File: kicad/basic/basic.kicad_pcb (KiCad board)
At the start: 2 copper layers, 50 x 50 mm, 20 parts, among them P2 CONN_01X15, P3 CONN_01X15, P4 CONN_01X06, P5 CONN_01X01, P6 CONN_01X01, P7 CONN_01X01, P8 CONN_01X01, P9 CONN_01X06, SW1 SW_PUSH, SW2 SW_PUSH

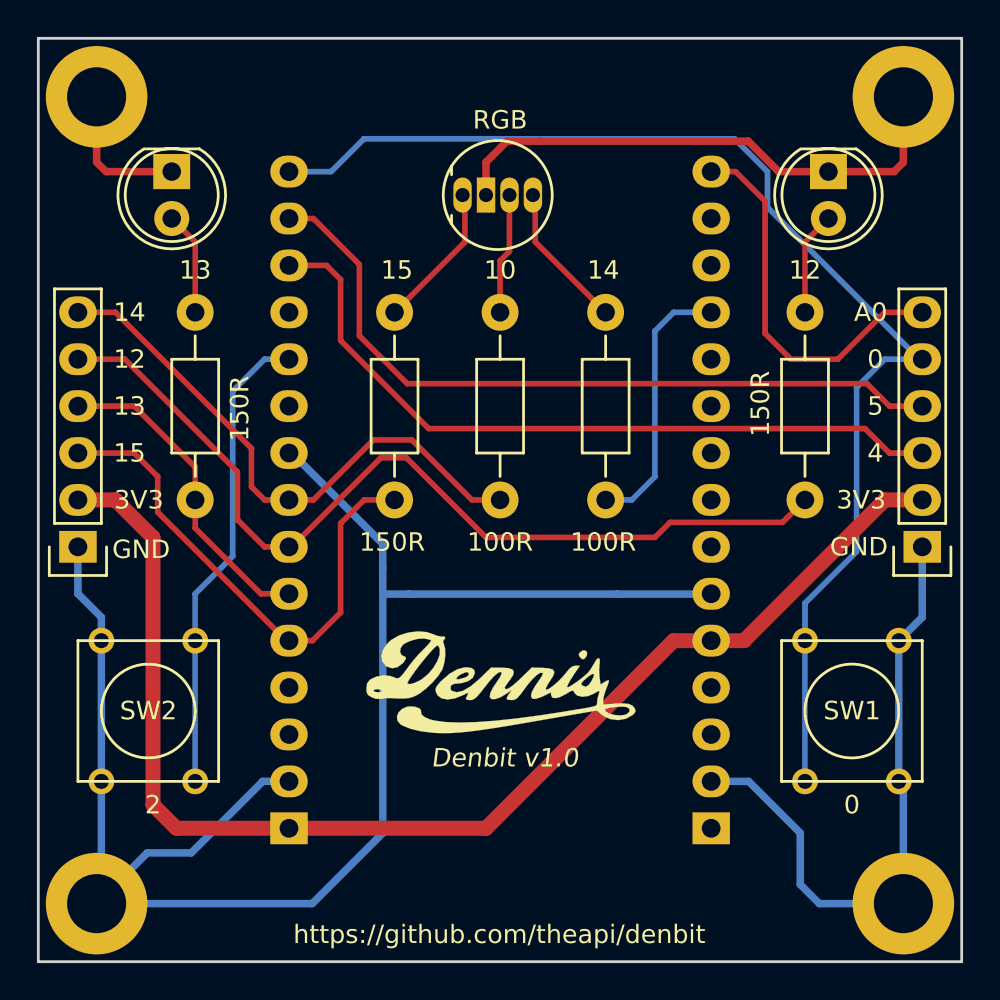
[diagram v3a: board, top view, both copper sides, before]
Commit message: Swap SDA & SCL on the header
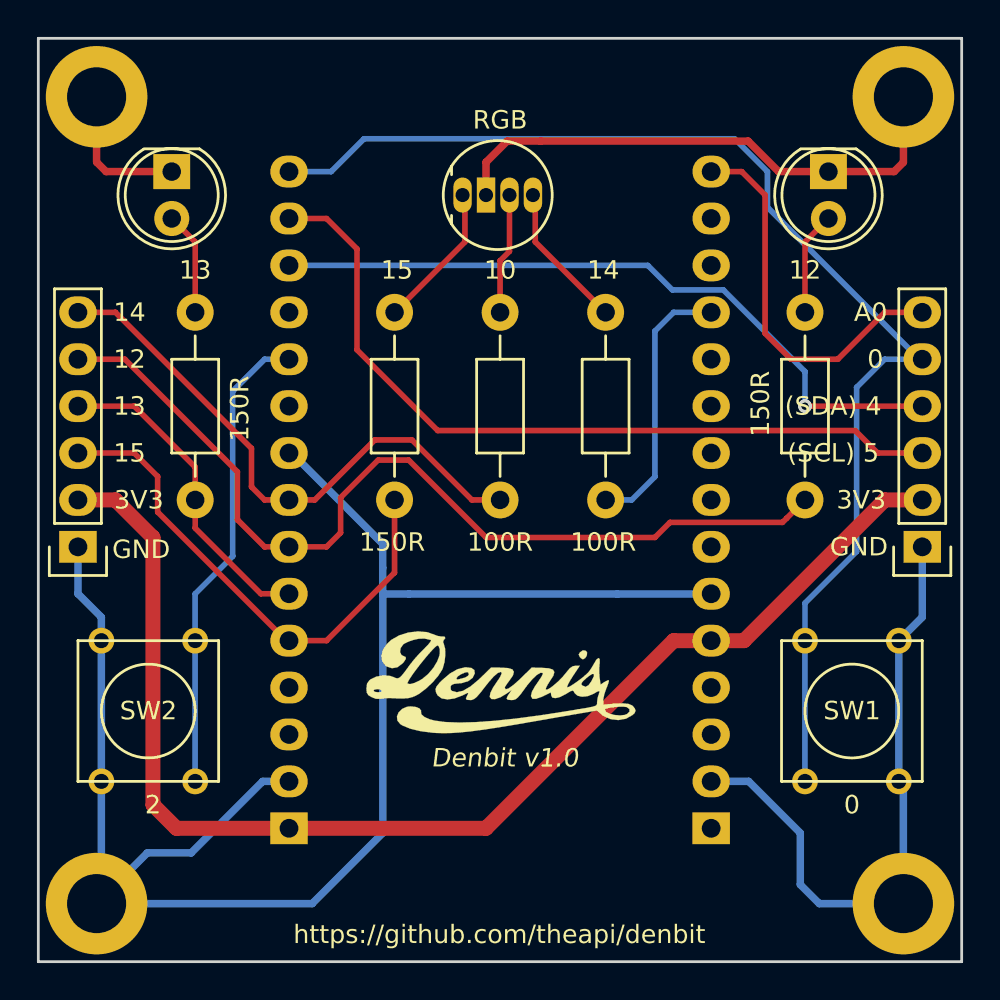
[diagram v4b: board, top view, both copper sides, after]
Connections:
- P4 pad 3: GPIO4 -> GPIO5
- P4 pad 4: GPIO5 -> GPIO4
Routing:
- net GPIO5: track 40.9 -> 42.9 mm
- net GPIO4: track 40.4 -> 38.5 mm, vias 0 -> 1
- net GPIO12: track 49.7 -> 51.1 mm
- net GPIO15: track 29.2 -> 28.1 mm
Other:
- board text added: "(SCL) 5"
- board text added: "(SDA) 4"
- board text removed: "4"
- board text removed: "5"

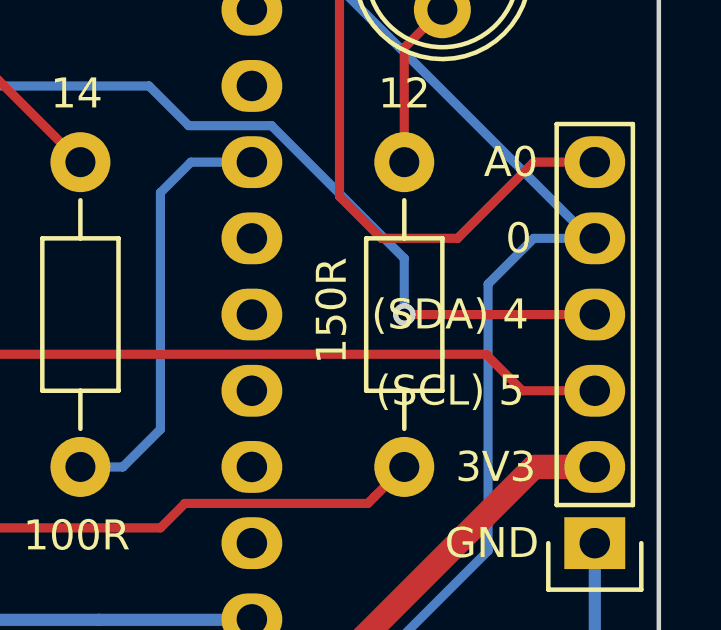
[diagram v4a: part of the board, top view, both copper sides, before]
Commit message: Tweaked labels
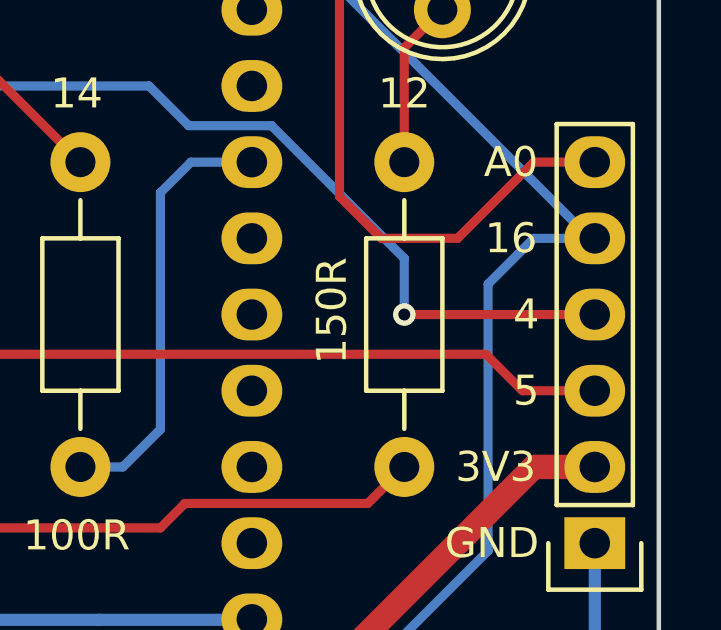
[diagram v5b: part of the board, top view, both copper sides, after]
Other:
- board text added: "16"
- board text added: "4"
- board text added: "5"
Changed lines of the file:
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@@
-(kicad_pcb (version 4) (host pcbnew 4.0.2-4+6225~38~ubuntu14.04.1-stable)
+(kicad_pcb (version 4) (host pcbnew 4.0.1-stable)
   (general
     (links 41)
     (no_connects 0)
-    (area 115.226999 66.712999 175.427001 126.913001)
+    (area 120.251999 71.737999 170.402001 121.888001)
     (thickness 1.6)
     (drawings 73)
@@
       (xy 4.255281 -1.532513) (xy 4.318 -1.651) (xy 4.481568 -1.764619) (xy 4.636344 -1.746168)) (layer F.SilkS) (width 0.01))
   )
-  (gr_text "(SDA) 4" (at 163.366 91.73) (layer F.SilkS)
+  (gr_text 4 (at 165.906 91.73) (layer F.SilkS)
     (effects (font (size 1 1) (thickness 0.15)))
   )
@@
     (effects (font (size 1 1) (thickness 0.15)) (justify mirror))
   )
-  (gr_text 0 (at 165.652 89.19) (layer B.SilkS)
+  (gr_text 16 (at 165.652 89.19) (layer B.SilkS)
     (effects (font (size 1 1) (thickness 0.15)) (justify mirror))
   )
@@
     (effects (font (size 1 1) (thickness 0.15)))
   )
-  (gr_text 0 (at 165.652 89.19) (layer F.SilkS)
+  (gr_text 16 (at 165.398 89.19) (layer F.SilkS)
     (effects (font (size 1 1) (thickness 0.15)))
   )
@@
     (effects (font (size 1 1) (thickness 0.15)) (justify mirror))
   )
-  (gr_text "(SCL) 5" (at 163.366 94.27) (layer F.SilkS)
-    (effects (font (size 1 1) (thickness 0.15)))
-  )
+  (gr_text 5 (at 165.906 94.27) (layer F.SilkS)
+    (effects (font (size 1 1) (thickness 0.15)))
+  )

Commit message: External power
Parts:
- added P1: EXT_PWR, Pin_Headers:Pin_Header_Straight_1x02, F.Cu at (144.1, 117.1)
- moved G*** 3.56 mm to (145.3, 103.2)
- moved G*** 1.02 mm to (145.3, 105.7)
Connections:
- P2 pad 1: Net-(P2-Pad1) -> VIN
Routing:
- net GND: track 164.4 -> 180.7 mm
- net VIN: track 0.00 -> 11.2 mm
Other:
- board text added: "4.5-10V"
- board text added: "ALT_PWR"

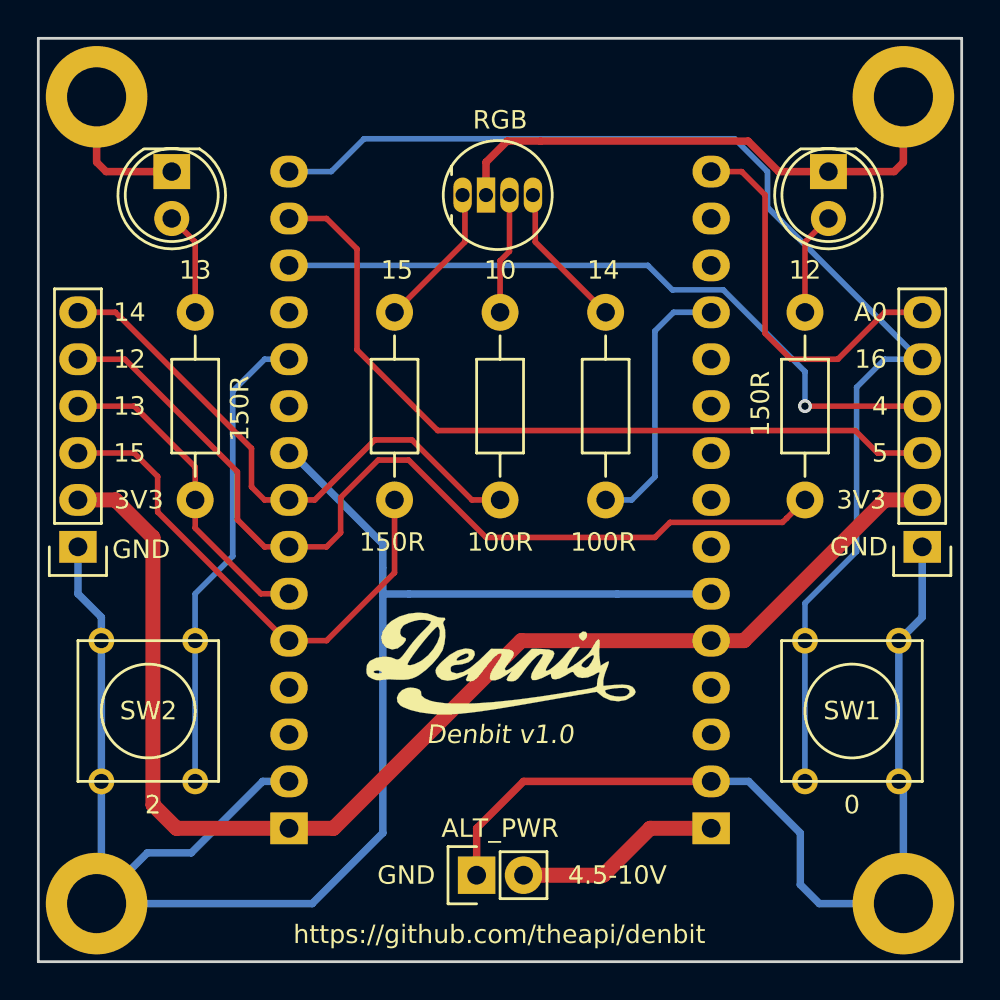
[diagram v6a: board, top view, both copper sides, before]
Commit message: Led position tweak & silkscreen adjustments
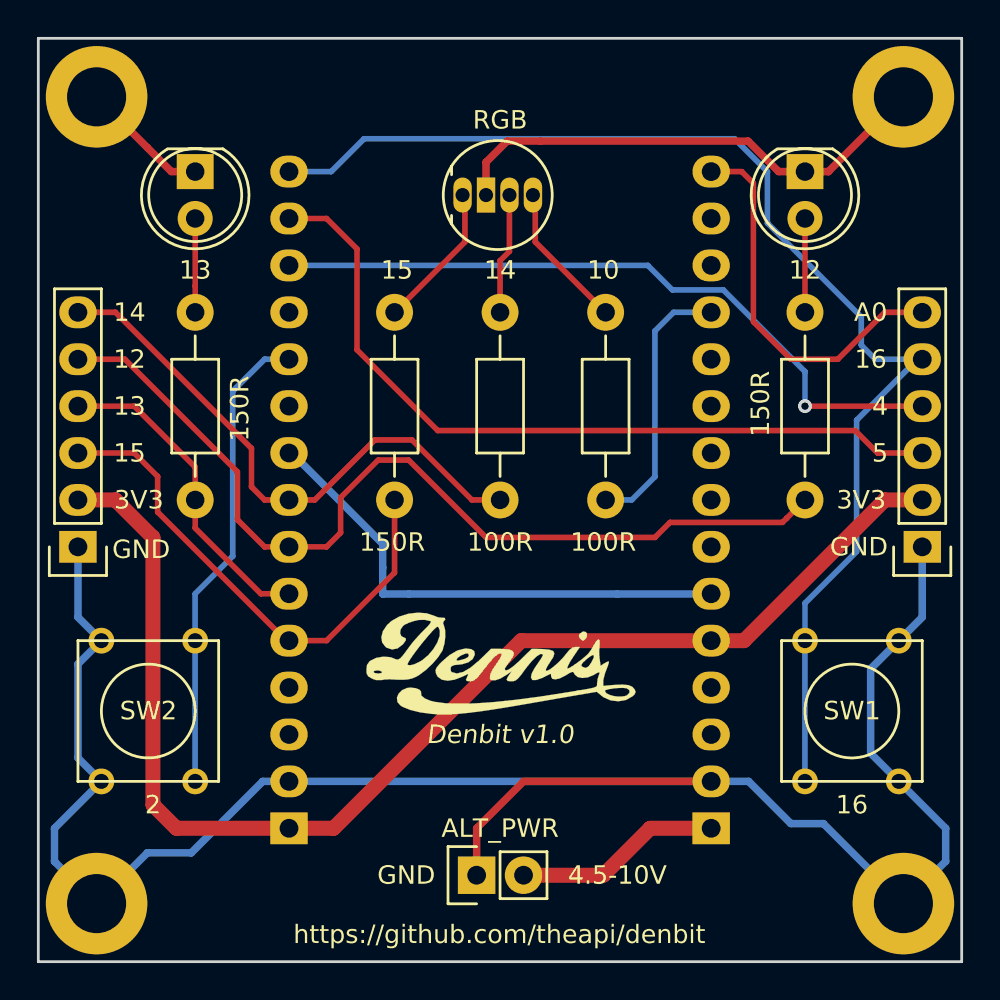
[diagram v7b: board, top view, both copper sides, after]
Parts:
- moved D1 1.27 mm to (128.8, 79.0)
- moved D4 1.27 mm to (161.8, 79.0)
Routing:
- net GND: track 180.7 -> 175.1 mm
- net /S_GREEN: track 5.61 -> 5.08 mm
- net /S_RED: track 5.61 -> 5.08 mm
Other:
- board text removed: "0"

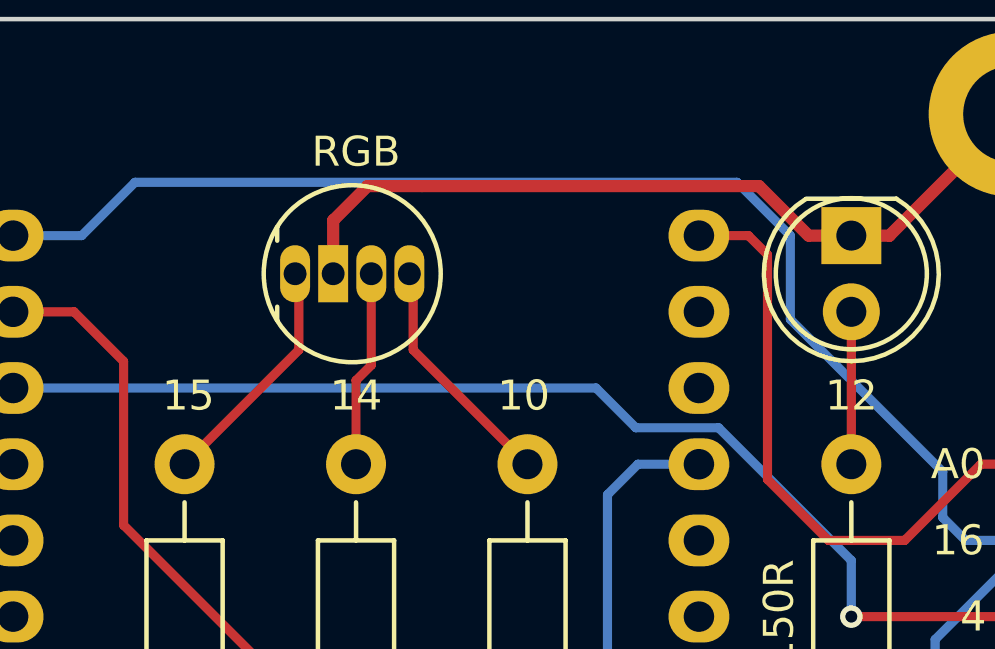
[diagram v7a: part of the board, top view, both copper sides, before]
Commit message: Staggered RGB led leads
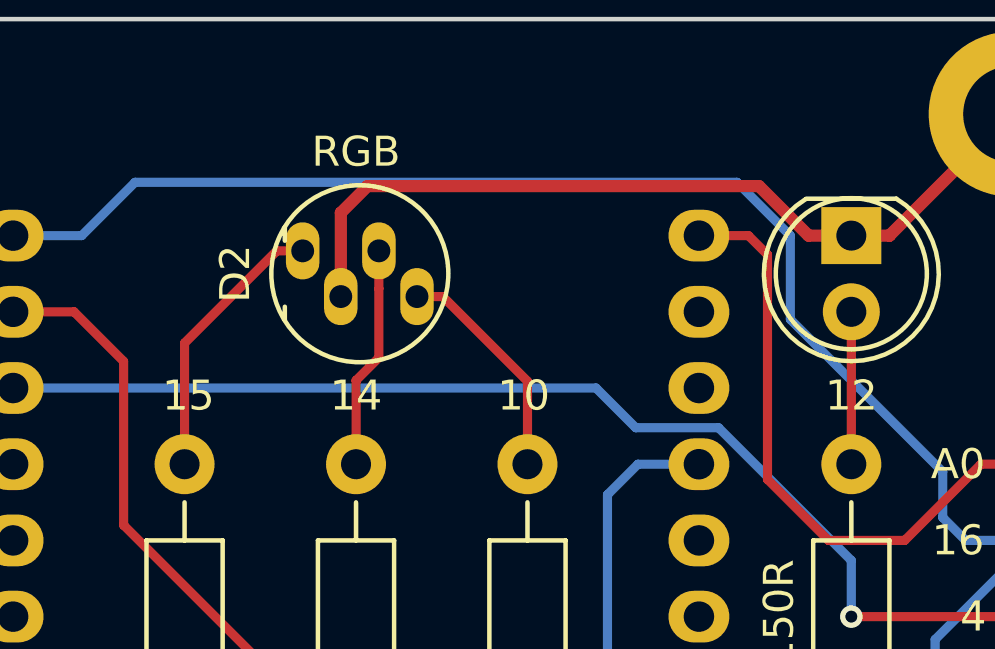
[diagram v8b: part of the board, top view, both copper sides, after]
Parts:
- moved D2 0.25 mm to (143.6, 80.3)
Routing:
- net /RGB_RED: track 7.93 -> 9.25 mm
- net /RGB_GREEN: track 6.56 -> 7.43 mm
- net GND: track 175.1 -> 175.7 mm
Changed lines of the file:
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@@
-(kicad_pcb (version 4) (host pcbnew 4.0.1-stable)
+(kicad_pcb (version 4) (host pcbnew 4.0.2-4+6225~38~ubuntu14.04.1-stable)
   (general
     (links 43)
@@
     (thickness 1.6)
     (drawings 76)
-    (tracks 168)
+    (tracks 170)
     (zones 0)
     (modules 21)
@@
     )
   )
-  (module LEDs:LED-RGB-5MM_Common_Cathode (layer F.Cu)
-    (at 143.3 80.3 90)
-    (descr "5mm common cathode RGB LED")
-    (tags "RGB LED 5mm Common Cathode")
-    (fp_text reference D2 (at 0 -2.25 90) (layer F.SilkS) hide
-      (effects (font (size 1 1) (thickness 0.15)))
-    )
-    (fp_text value LED_RCBG (at 0 6.25 90) (layer F.Fab)
-      (effects (font (size 1 1) (thickness 0.15)))
-    )
-    (fp_circle (center 0 1.905) (end 3.2 1.905) (layer F.CrtYd) (width 0.05))
-    (fp_line (start -1.1 -0.595) (end -1.55 -0.595) (layer F.SilkS) (width 0.15))
-    (fp_circle (center 0 1.905) (end 2.95 1.905) (layer F.SilkS) (width 0.15))
-    (fp_line (start 1.1 -0.595) (end 1.55 -0.595) (layer F.SilkS) (width 0.15))
-    (pad 1 thru_hole oval (at 0 0 90) (size 1.905 1) (drill 0.762) (layers *.Cu *.Mask F.SilkS)
-      (net 13 /RGB_RED))
-    (pad 2 thru_hole rect (at 0 1.27 90) (size 1.905 1) (drill 0.762) (layers *.Cu *.Mask F.SilkS)
-      (net 1 GND))
-    (pad 3 thru_hole oval (at 0 2.54 90) (size 1.905 1) (drill 0.762) (layers *.Cu *.Mask F.SilkS)
-      (net 14 /RGB_GREEN))
-    (pad 4 thru_hole oval (at 0 3.81 90) (size 1.905 1) (drill 0.762) (layers *.Cu *.Mask F.SilkS)
-      (net 15 /RGB_BLUE))
-  )
   (module denbit:LOGO (layer F.Cu)
     (at 145.332 105.7)
@@
     )
   )
+  (module LEDs:LED-RGB-5MM_Common_Cathode (layer F.Cu)
+    (at 143.554 80.3 90)
+    (descr "5mm common cathode RGB LED")
+    (tags "RGB LED 5mm Common Cathode")
+    (fp_text reference D2 (at 0 -2.25 90) (layer F.SilkS)
+      (effects (font (size 1 1) (thickness 0.15)))
+    )
+    (fp_text value LED_RCBG (at 0 6.25 90) (layer F.Fab)
+      (effects (font (size 1 1) (thickness 0.15)))
+    )
+    (fp_circle (center 0 1.905) (end 3.2 1.905) (layer F.CrtYd) (width 0.05))
+    (fp_line (start -1.1 -0.595) (end -1.55 -0.595) (layer F.SilkS) (width 0.15))
+    (fp_circle (center 0 1.905) (end 2.95 1.905) (layer F.SilkS) (width 0.15))
+    (fp_line (start 1.1 -0.595) (end 1.55 -0.595) (layer F.SilkS) (width 0.15))
+    (pad 1 thru_hole oval (at 0.762 0 90) (size 1.905 1.1176) (drill 0.762) (layers *.Cu *.Mask F.SilkS)
+      (net 13 /RGB_RED))
+    (pad 2 thru_hole oval (at -0.762 1.27 90) (size 1.905 1.1176) (drill 0.762) (layers *.Cu *.Mask F.SilkS)
+      (net 1 GND))
+    (pad 3 thru_hole oval (at 0.762 2.54 90) (size 1.905 1.1176) (drill 0.762) (layers *.Cu *.Mask F.SilkS)
+      (net 14 /RGB_GREEN))
+    (pad 4 thru_hole oval (at -0.762 3.81 90) (size 1.905 1.1176) (drill 0.762) (layers *.Cu *.Mask F.SilkS)
+      (net 15 /RGB_BLUE))
+  )
   (gr_text 4.5-10V (at 151.682 117.13) (layer B.SilkS)
     (effects (font (size 1 1) (thickness 0.15)) (justify mirror))
@@
   (gr_line (start 170.327 121.813) (end 120.327 121.813) (angle 90) (layer Edge.Cuts) (width 0.15))
   (gr_line (start 170.327 71.813) (end 170.327 121.813) (angle 90) (layer Edge.Cuts) (width 0.15))
+  (segment (start 144.824 78.268) (end 144.824 81.062) (width 0.406) (layer F.Cu) (net 1))
+  (segment (start 163.112 79.03) (end 160.416 79.03) (width 0.406) (layer F.Cu) (net 1))
+  (segment (start 160.416 79.03) (end 158.765 77.379) (width 0.406) (layer F.Cu) (net 1))
+  (segment (start 158.765 77.379) (end 145.713 77.379) (width 0.406) (layer F.Cu) (net 1))
+  (segment (start 145.713 77.379) (end 144.824 78.268) (width 0.406) (layer F.Cu) (net 1))
   (segment (start 123.742 104.43) (end 122.472 103.16) (width 0.406) (layer B.Cu) (net 1))
   (segment (start 122.472 103.16) (end 122.472 99.35) (width 0.406) (layer B.Cu) (net 1))
@@
   (segment (start 126.232999 115.919001) (end 123.483 118.669) (width 0.406) (layer B.Cu) (net 1))
   (segment (start 133.902 112.05) (end 132.48 112.05) (width 0.406) (layer B.Cu) (net 1))
-  (segment (start 147.5295 77.379) (end 145.713 77.379) (width 0.406) (layer F.Cu) (net 1))
-  (segment (start 147.5295 77.379) (end 158.765 77.379) (width 0.406) (layer F.Cu) (net 1))
-  (segment (start 158.765 77.379) (end 160.416 79.03) (width 0.406) (layer F.Cu) (net 1))
-  (segment (start 163.112 79.03) (end 160.416 79.03) (width 0.406) (layer F.Cu) (net 1))
-  (segment (start 144.57 78.522) (end 144.57 80.3) (width 0.406) (layer F.Cu) (net 1))
-  (segment (start 145.713 77.379) (end 144.57 78.522) (width 0.406) (layer F.Cu) (net 1))
   (segment (start 163.112 79.03) (end 163.122 79.03) (width 0.406) (layer F.Cu) (net 1))
   (segment (start 133.902 94.27) (end 133.7496 94.27) (width 0.406) (layer F.Cu) (net 1))
@@
   (segment (start 128.822 86.65) (end 128.822 85.236508) (width 0.305) (layer F.Cu) (net 12))
   (segment (start 128.822 85.236508) (end 128.822 81.57) (width 0.305) (layer F.Cu) (net 12))
-  (segment (start 143.427 82.84) (end 143.427 80.3) (width 0.305) (layer F.Cu) (net 13))
-  (segment (start 139.617 86.65) (end 143.427 82.84) (width 0.305) (layer F.Cu) (net 13))
-  (segment (start 145.84 83.348) (end 145.84 80.3) (width 0.305) (layer F.Cu) (net 14))
+  (segment (start 139.617 86.65) (end 139.617 82.6112) (width 0.305) (layer F.Cu) (net 13))
+  (segment (start 139.617 82.6112) (end 142.6902 79.538) (width 0.305) (layer F.Cu) (net 13))
+  (segment (start 142.6902 79.538) (end 143.554 79.538) (width 0.305) (layer F.Cu) (net 13))
   (segment (start 145.332 86.65) (end 145.332 83.856) (width 0.305) (layer F.Cu) (net 14))
-  (segment (start 145.332 83.856) (end 145.84 83.348) (width 0.305) (layer F.Cu) (net 14))
-  (segment (start 151.047 86.65) (end 147.237 82.84) (width 0.305) (layer F.Cu) (net 15))
-  (segment (start 147.237 82.84) (end 147.237 80.3) (width 0.305) (layer F.Cu) (net 15))
+  (segment (start 145.332 83.856) (end 146.094 83.094) (width 0.305) (layer F.Cu) (net 14))
+  (segment (start 146.094 83.094) (end 146.094 80.7955) (width 0.305) (layer F.Cu) (net 14))
+  (segment (start 146.094 80.7955) (end 146.094 79.538) (width 0.305) (layer F.Cu) (net 14))
+  (segment (start 151.047 86.65) (end 151.047 83.8812) (width 0.305) (layer F.Cu) (net 15))
+  (segment (start 151.047 83.8812) (end 148.2278 81.062) (width 0.305) (layer F.Cu) (net 15))
+  (segment (start 148.2278 81.062) (end 147.364 81.062) (width 0.305) (layer F.Cu) (net 15))
   (segment (start 161.842 81.57) (end 161.842 86.65) (width 0.305) (layer F.Cu) (net 16))
   (segment (start 151.047 96.81) (end 152.460492 96.81) (width 0.305) (layer B.Cu) (net 19))
